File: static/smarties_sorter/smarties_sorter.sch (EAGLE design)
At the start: 17 parts, among them IC1 MEGA8-P, Q1 16Mhz, Q2 IRLZ44Z

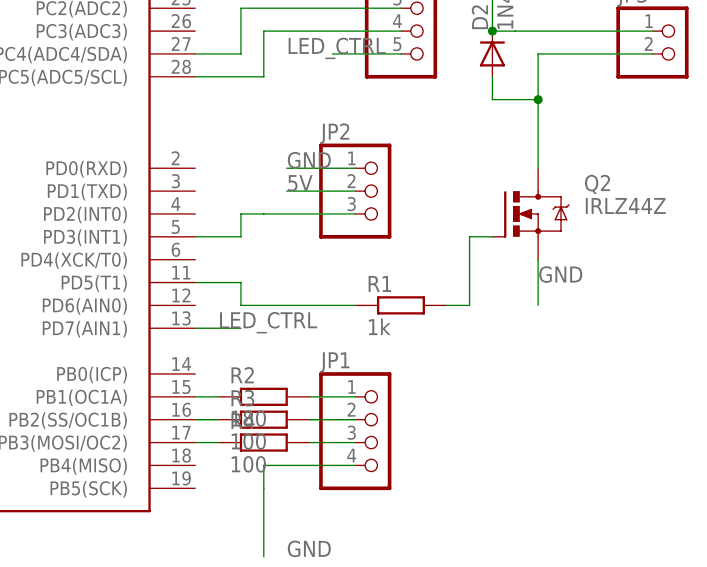
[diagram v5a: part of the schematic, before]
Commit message: [Smarties_sorter] Adds resistor to pull down motor command
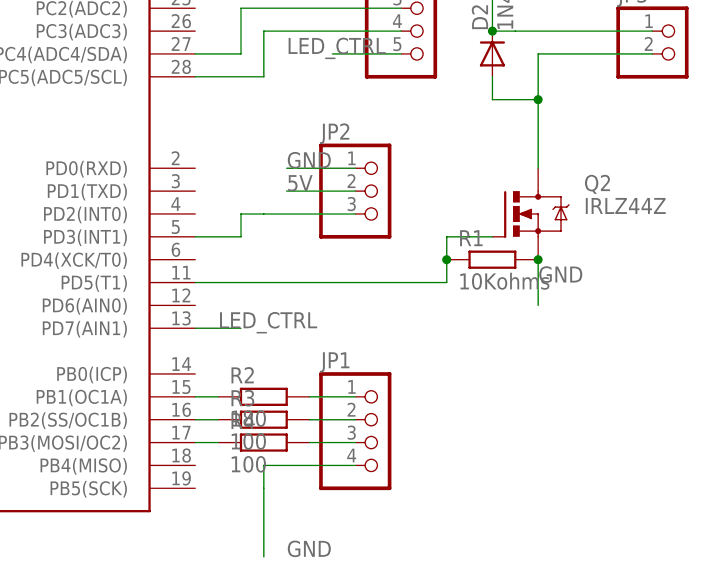
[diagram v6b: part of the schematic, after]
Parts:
- R1: value 1k -> 10Kohms; device resistor:R-EU_0411/12 -> rcl:R-EU_0414/15
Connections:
- removed net N$8: Q2.G, R1.2
- net GND: now also R1.2
- net N$9: now also Q2.G
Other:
- moved on the sheet: R1
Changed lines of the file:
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@@
 <part name="Q2" library="transistor-power" deviceset="IRLZ44Z" device=""/>
 <part name="JP3" library="pinhead" deviceset="PINHD-1X2" device=""/>
-<part name="R1" library="resistor" deviceset="R-EU_" device="0411/12" value="1k"/>
 <part name="R2" library="resistor" deviceset="R-EU_" device="0411/12" value="180"/>
 <part name="R3" library="resistor" deviceset="R-EU_" device="0411/12" value="100"/>
@@
 <part name="C3" library="capacitor-wima" deviceset="C" device="5/3" value="200nF"/>
 <part name="JP4" library="pinhead" deviceset="PINHD-1X5" device=""/>
+<part name="R1" library="rcl" deviceset="R-EU_" device="0414/15" value="10Kohms"/>
 </parts>
 <sheets>
@@
 <instance part="Q2" gate="G$1" x="88.9" y="55.88"/>
 <instance part="JP3" gate="G$1" x="106.68" y="73.66"/>
-<instance part="R1" gate="G$1" x="76.2" y="45.72"/>
 <instance part="R2" gate="G$1" x="60.96" y="35.56"/>
 <instance part="R3" gate="G$1" x="60.96" y="33.02"/>
@@
 <instance part="C3" gate="G$1" x="-5.08" y="78.74"/>
 <instance part="JP4" gate="A" x="78.74" y="78.74"/>
+<instance part="R1" gate="G$1" x="86.36" y="50.8"/>
 </instances>
 <busses>
@@
 <wire x1="91.44" y1="50.8" x2="91.44" y2="45.72" width="0.1524" layer="91"/>
 <label x="91.44" y="48.26" size="1.778" layer="95"/>
+<pinref part="R1" gate="G$1" pin="2"/>
+<junction x="91.44" y="50.8"/>
 </segment>
 <segment>
@@
 </segment>
 </net>
-<net name="N$8" class="0">
+<net name="N$9" class="0">
 <segment>
+<pinref part="IC1" gate="G$1" pin="PD5(T1)"/>
+<wire x1="58.42" y1="48.26" x2="53.34" y2="48.26" width="0.1524" layer="91"/>
+<wire x1="58.42" y1="48.26" x2="81.28" y2="48.26" width="0.1524" layer="91"/>
+<wire x1="81.28" y1="48.26" x2="81.28" y2="50.8" width="0.1524" layer="91"/>
 <pinref part="Q2" gate="G$1" pin="G"/>
+<wire x1="81.28" y1="50.8" x2="81.28" y2="53.34" width="0.1524" layer="91"/>
 <wire x1="86.36" y1="53.34" x2="83.82" y2="53.34" width="0.1524" layer="91"/>
-<wire x1="83.82" y1="53.34" x2="83.82" y2="45.72" width="0.1524" layer="91"/>
-<pinref part="R1" gate="G$1" pin="2"/>
-<wire x1="83.82" y1="45.72" x2="81.28" y2="45.72" width="0.1524" layer="91"/>
+<wire x1="81.28" y1="53.34" x2="83.82" y2="53.34" width="0.1524" layer="91"/>
+<pinref part="R1" gate="G$1" pin="1"/>
+<junction x="81.28" y="50.8"/>
 </segment>
 </net>
-<net name="N$9" class="0">
-<segment>
-<pinref part="R1" gate="G$1" pin="1"/>
-<wire x1="71.12" y1="45.72" x2="58.42" y2="45.72" width="0.1524" layer="91"/>
-<wire x1="58.42" y1="45.72" x2="58.42" y2="48.26" width="0.1524" layer="91"/>
-<pinref part="IC1" gate="G$1" pin="PD5(T1)"/>
-<wire x1="58.42" y1="48.26" x2="53.34" y2="48.26" width="0.1524" layer="91"/>
-</segment>
-</net>

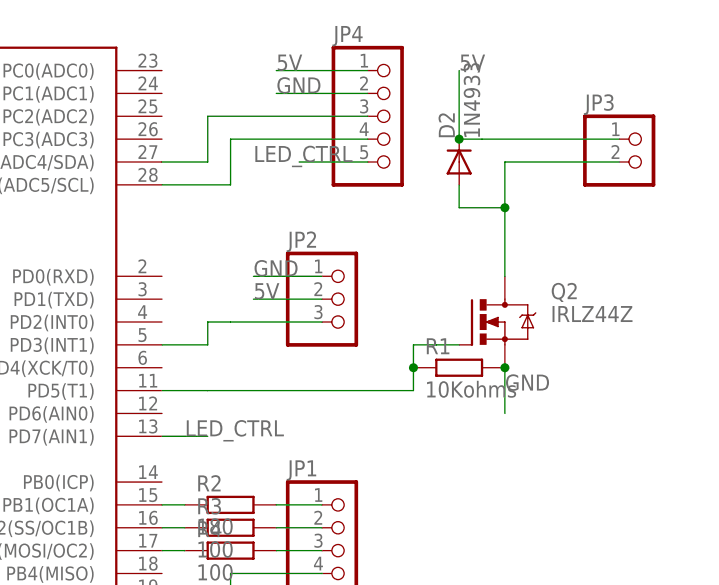
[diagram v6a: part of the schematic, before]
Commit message: [smarties_sorter] Adds UART plug
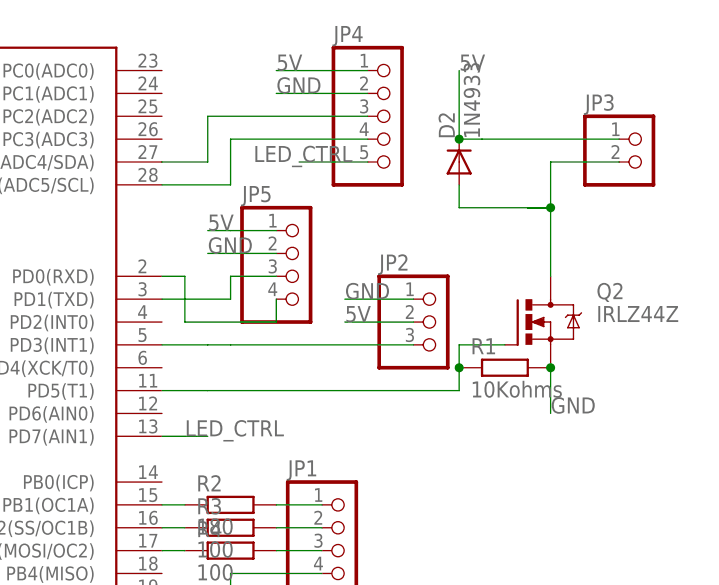
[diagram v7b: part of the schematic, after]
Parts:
- added JP5: (no value), pinhead:PINHD-1X4
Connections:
- new net N$13: IC1.PD0(RXD), JP5.4
- new net N$8: IC1.PD1(TXD), JP5.3
- net 5V: now also JP5.1
- net GND: now also JP5.2
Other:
- moved on the sheet: JP2, Q2, R1
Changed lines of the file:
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@@
 <part name="JP4" library="pinhead" deviceset="PINHD-1X5" device=""/>
 <part name="R1" library="rcl" deviceset="R-EU_" device="0414/15" value="10Kohms"/>
+<part name="JP5" library="pinhead" deviceset="PINHD-1X4" device=""/>
 </parts>
 <sheets>
@@
 <instance part="Q1" gate="G$1" x="-7.62" y="63.5" rot="R90"/>
 <instance part="JP1" gate="A" x="73.66" y="30.48"/>
-<instance part="JP2" gate="A" x="73.66" y="58.42"/>
-<instance part="Q2" gate="G$1" x="88.9" y="55.88"/>
+<instance part="JP2" gate="A" x="83.82" y="55.88"/>
+<instance part="Q2" gate="G$1" x="93.98" y="55.88"/>
 <instance part="JP3" gate="G$1" x="106.68" y="73.66"/>
 <instance part="R2" gate="G$1" x="60.96" y="35.56"/>
@@
 <instance part="C3" gate="G$1" x="-5.08" y="78.74"/>
 <instance part="JP4" gate="A" x="78.74" y="78.74"/>
-<instance part="R1" gate="G$1" x="86.36" y="50.8"/>
+<instance part="R1" gate="G$1" x="91.44" y="50.8"/>
+<instance part="JP5" gate="A" x="68.58" y="60.96"/>
 </instances>
 <busses>
@@
 <segment>
 <pinref part="JP2" gate="A" pin="1"/>
-<wire x1="71.12" y1="60.96" x2="63.5" y2="60.96" width="0.1524" layer="91"/>
-<label x="63.5" y="60.96" size="1.778" layer="95"/>
+<wire x1="81.28" y1="58.42" x2="73.66" y2="58.42" width="0.1524" layer="91"/>
+<label x="73.66" y="58.42" size="1.778" layer="95"/>
 </segment>
 <segment>
 <pinref part="Q2" gate="G$1" pin="S"/>
-<wire x1="91.44" y1="50.8" x2="91.44" y2="45.72" width="0.1524" layer="91"/>
-<label x="91.44" y="48.26" size="1.778" layer="95"/>
+<wire x1="96.52" y1="50.8" x2="96.52" y2="45.72" width="0.1524" layer="91"/>
+<label x="96.52" y="45.72" size="1.778" layer="95"/>
 <pinref part="R1" gate="G$1" pin="2"/>
-<junction x="91.44" y="50.8"/>
+<junction x="96.52" y="50.8"/>
 </segment>
 <segment>
@@
 <label x="66.04" y="81.28" size="1.778" layer="95"/>
 </segment>
+<segment>
+<pinref part="JP5" gate="A" pin="2"/>
+<wire x1="66.04" y1="63.5" x2="60.96" y2="63.5" width="0.1524" layer="91"/>
+<label x="58.42" y="63.5" size="1.778" layer="95"/>
+<wire x1="60.96" y1="63.5" x2="58.42" y2="63.5" width="0.1524" layer="91"/>
+</segment>
 </net>
 <net name="5V" class="0">
 <segment>
 <pinref part="JP2" gate="A" pin="2"/>
-<wire x1="71.12" y1="58.42" x2="63.5" y2="58.42" width="0.1524" layer="91"/>
-<label x="63.5" y="58.42" size="1.778" layer="95"/>
+<wire x1="81.28" y1="55.88" x2="73.66" y2="55.88" width="0.1524" layer="91"/>
+<label x="73.66" y="55.88" size="1.778" layer="95"/>
 </segment>
 <segment>
@@
 <label x="66.04" y="83.82" size="1.778" layer="95"/>
 </segment>
+<segment>
+<pinref part="JP5" gate="A" pin="1"/>
+<wire x1="66.04" y1="66.04" x2="60.96" y2="66.04" width="0.1524" layer="91"/>
+<label x="58.42" y="66.04" size="1.778" layer="95"/>
+<wire x1="60.96" y1="66.04" x2="58.42" y2="66.04" width="0.1524" layer="91"/>
+</segment>
 </net>
 <net name="N$6" class="0">
@@
 <pinref part="JP2" gate="A" pin="3"/>
 <pinref part="IC1" gate="G$1" pin="PD3(INT1)"/>
-<wire x1="71.12" y1="55.88" x2="60.96" y2="55.88" width="0.1524" layer="91"/>
-<wire x1="60.96" y1="55.88" x2="58.42" y2="55.88" width="0.1524" layer="91"/>
-<wire x1="58.42" y1="55.88" x2="58.42" y2="53.34" width="0.1524" layer="91"/>
+<wire x1="81.28" y1="53.34" x2="60.96" y2="53.34" width="0.1524" layer="91"/>
+<wire x1="60.96" y1="53.34" x2="58.42" y2="53.34" width="0.1524" layer="91"/>
 <wire x1="58.42" y1="53.34" x2="53.34" y2="53.34" width="0.1524" layer="91"/>
 </segment>
@@
 <pinref part="JP3" gate="G$1" pin="2"/>
 <pinref part="Q2" gate="G$1" pin="D"/>
-<wire x1="104.14" y1="73.66" x2="91.44" y2="73.66" width="0.1524" layer="91"/>
-<wire x1="91.44" y1="73.66" x2="91.44" y2="68.58" width="0.1524" layer="91"/>
-<wire x1="91.44" y1="68.58" x2="91.44" y2="60.96" width="0.1524" layer="91"/>
-<wire x1="91.44" y1="68.58" x2="86.36" y2="68.58" width="0.1524" layer="91"/>
+<wire x1="104.14" y1="73.66" x2="96.52" y2="73.66" width="0.1524" layer="91"/>
+<wire x1="96.52" y1="73.66" x2="96.52" y2="68.58" width="0.1524" layer="91"/>
+<wire x1="96.52" y1="68.58" x2="93.98" y2="68.58" width="0.1524" layer="91"/>
+<wire x1="93.98" y1="68.58" x2="96.52" y2="68.58" width="0.1524" layer="91"/>
+<wire x1="96.52" y1="68.58" x2="96.52" y2="60.96" width="0.1524" layer="91"/>
+<wire x1="96.52" y1="68.58" x2="93.98" y2="68.58" width="0.1524" layer="91"/>
+<wire x1="93.98" y1="68.58" x2="86.36" y2="68.58" width="0.1524" layer="91"/>
 <wire x1="86.36" y1="68.58" x2="86.36" y2="71.12" width="0.1524" layer="91"/>
 <pinref part="D2" gate="1" pin="A"/>
-<junction x="91.44" y="68.58"/>
+<junction x="96.52" y="68.58"/>
 </segment>
 </net>
@@
 <pinref part="IC1" gate="G$1" pin="PD5(T1)"/>
 <wire x1="58.42" y1="48.26" x2="53.34" y2="48.26" width="0.1524" layer="91"/>
-<wire x1="58.42" y1="48.26" x2="81.28" y2="48.26" width="0.1524" layer="91"/>
-<wire x1="81.28" y1="48.26" x2="81.28" y2="50.8" width="0.1524" layer="91"/>
+<wire x1="58.42" y1="48.26" x2="86.36" y2="48.26" width="0.1524" layer="91"/>
+<wire x1="86.36" y1="48.26" x2="86.36" y2="50.8" width="0.1524" layer="91"/>
 <pinref part="Q2" gate="G$1" pin="G"/>
-<wire x1="81.28" y1="50.8" x2="81.28" y2="53.34" width="0.1524" layer="91"/>
-<wire x1="86.36" y1="53.34" x2="83.82" y2="53.34" width="0.1524" layer="91"/>
-<wire x1="81.28" y1="53.34" x2="83.82" y2="53.34" width="0.1524" layer="91"/>
+<wire x1="86.36" y1="50.8" x2="86.36" y2="53.34" width="0.1524" layer="91"/>
+<wire x1="91.44" y1="53.34" x2="86.36" y2="53.34" width="0.1524" layer="91"/>
 <pinref part="R1" gate="G$1" pin="1"/>
-<junction x="81.28" y="50.8"/>
+<junction x="86.36" y="50.8"/>
 </segment>
 </net>
@@
 </segment>
 </net>
+<net name="N$8" class="0">
+<segment>
+<pinref part="IC1" gate="G$1" pin="PD1(TXD)"/>
+<wire x1="53.34" y1="58.42" x2="60.96" y2="58.42" width="0.1524" layer="91"/>
+<wire x1="60.96" y1="58.42" x2="60.96" y2="60.96" width="0.1524" layer="91"/>
+<pinref part="JP5" gate="A" pin="3"/>
+<wire x1="60.96" y1="60.96" x2="66.04" y2="60.96" width="0.1524" layer="91"/>
+</segment>
+</net>
+<net name="N$13" class="0">
+<segment>
+<pinref part="JP5" gate="A" pin="4"/>
+<wire x1="66.04" y1="58.42" x2="66.04" y2="55.88" width="0.1524" layer="91"/>
+<wire x1="66.04" y1="55.88" x2="55.88" y2="55.88" width="0.1524" layer="91"/>
+<wire x1="55.88" y1="55.88" x2="55.88" y2="60.96" width="0.1524" layer="91"/>
+<pinref part="IC1" gate="G$1" pin="PD0(RXD)"/>
+<wire x1="55.88" y1="60.96" x2="53.34" y2="60.96" width="0.1524" layer="91"/>
+</segment>
+</net>

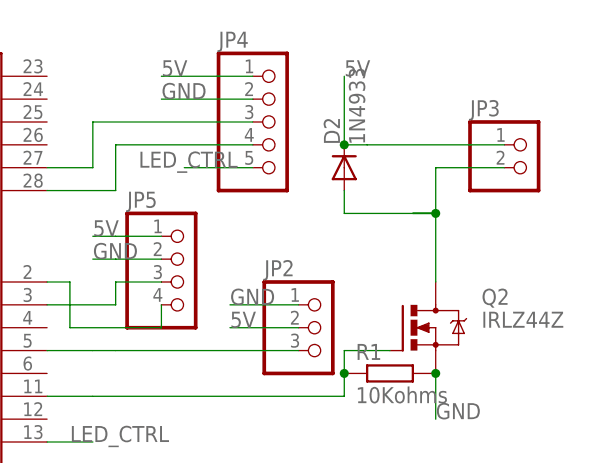
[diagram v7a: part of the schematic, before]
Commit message: [smarties_sorter] Adds capa on the motor
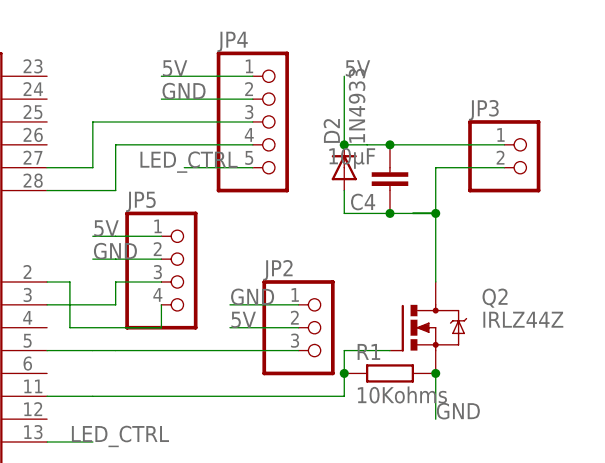
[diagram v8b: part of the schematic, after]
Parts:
- added C4: 10µF, capacitor-wima:C5/5
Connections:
- net 5V: now also C4.2
- net N$7: now also C4.1
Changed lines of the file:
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@@
 <part name="R1" library="rcl" deviceset="R-EU_" device="0414/15" value="10Kohms"/>
 <part name="JP5" library="pinhead" deviceset="PINHD-1X4" device=""/>
+<part name="C4" library="capacitor-wima" deviceset="C" device="5/5" value="10µF"/>
 </parts>
 <sheets>
@@
 <instance part="R1" gate="G$1" x="91.44" y="50.8"/>
 <instance part="JP5" gate="A" x="68.58" y="60.96"/>
+<instance part="C4" gate="G$1" x="91.44" y="71.12" rot="R180"/>
 </instances>
 <busses>
@@
 <segment>
 <pinref part="JP3" gate="G$1" pin="1"/>
-<wire x1="104.14" y1="76.2" x2="88.9" y2="76.2" width="0.1524" layer="91"/>
+<wire x1="104.14" y1="76.2" x2="91.44" y2="76.2" width="0.1524" layer="91"/>
 <label x="86.36" y="83.82" size="1.778" layer="95"/>
+<wire x1="91.44" y1="76.2" x2="88.9" y2="76.2" width="0.1524" layer="91"/>
 <wire x1="88.9" y1="76.2" x2="86.36" y2="76.2" width="0.1524" layer="91"/>
 <wire x1="86.36" y1="76.2" x2="86.36" y2="83.82" width="0.1524" layer="91"/>
 <pinref part="D2" gate="1" pin="C"/>
 <junction x="86.36" y="76.2"/>
+<pinref part="C4" gate="G$1" pin="2"/>
+<junction x="91.44" y="76.2"/>
 </segment>
 <segment>
@@
 <wire x1="96.52" y1="68.58" x2="96.52" y2="60.96" width="0.1524" layer="91"/>
 <wire x1="96.52" y1="68.58" x2="93.98" y2="68.58" width="0.1524" layer="91"/>
-<wire x1="93.98" y1="68.58" x2="86.36" y2="68.58" width="0.1524" layer="91"/>
+<wire x1="93.98" y1="68.58" x2="91.44" y2="68.58" width="0.1524" layer="91"/>
+<wire x1="91.44" y1="68.58" x2="86.36" y2="68.58" width="0.1524" layer="91"/>
 <wire x1="86.36" y1="68.58" x2="86.36" y2="71.12" width="0.1524" layer="91"/>
 <pinref part="D2" gate="1" pin="A"/>
 <junction x="96.52" y="68.58"/>
+<pinref part="C4" gate="G$1" pin="1"/>
+<junction x="91.44" y="68.58"/>
 </segment>
 </net>
